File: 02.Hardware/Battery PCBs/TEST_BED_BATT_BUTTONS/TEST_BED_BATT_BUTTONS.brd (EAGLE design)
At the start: 25.2 x 30.9 mm, 9 parts

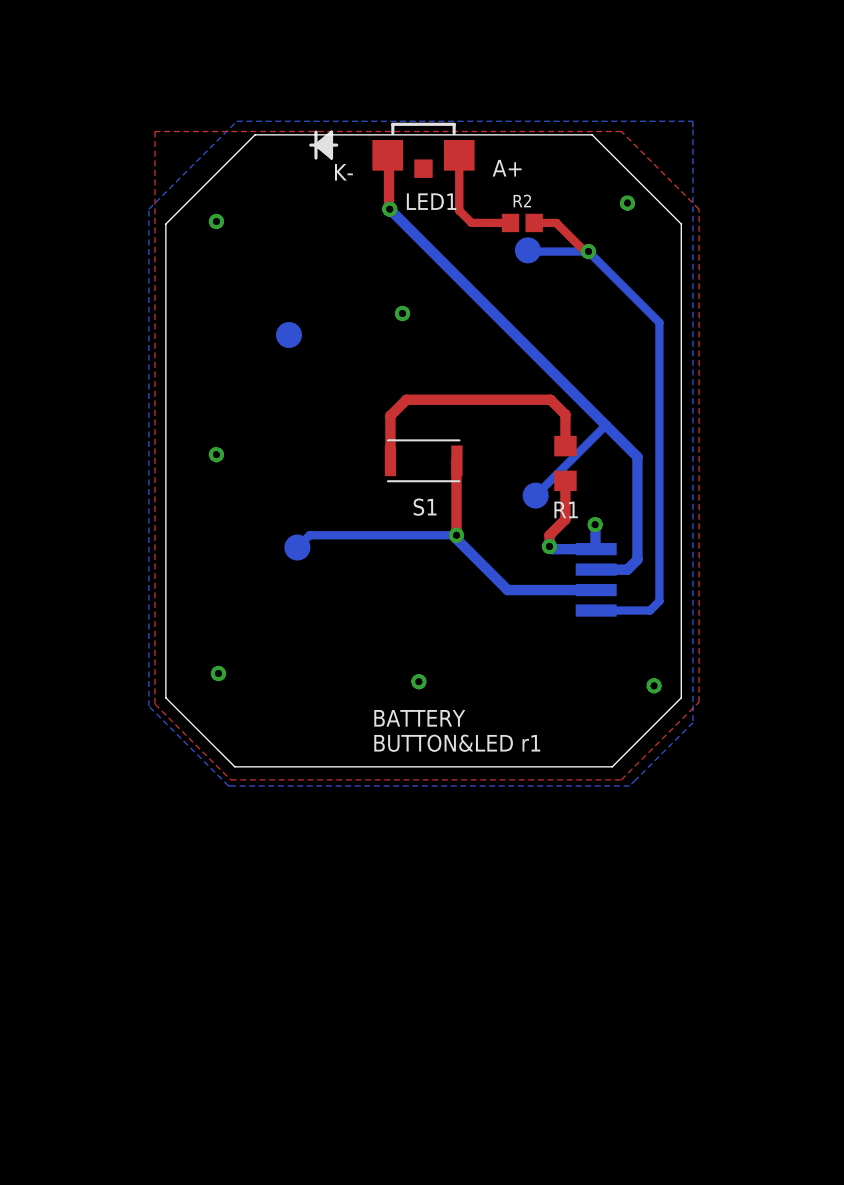
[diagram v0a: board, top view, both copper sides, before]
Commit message: Cambios revisados con David
Revision de los pcbs de la bateria.

En el DCDC se añade un diode Clamp (bat54s) en la medicion de la tension de salida.
Actualizacion de la BOM a v8.
Documentos de Cambios de versiones
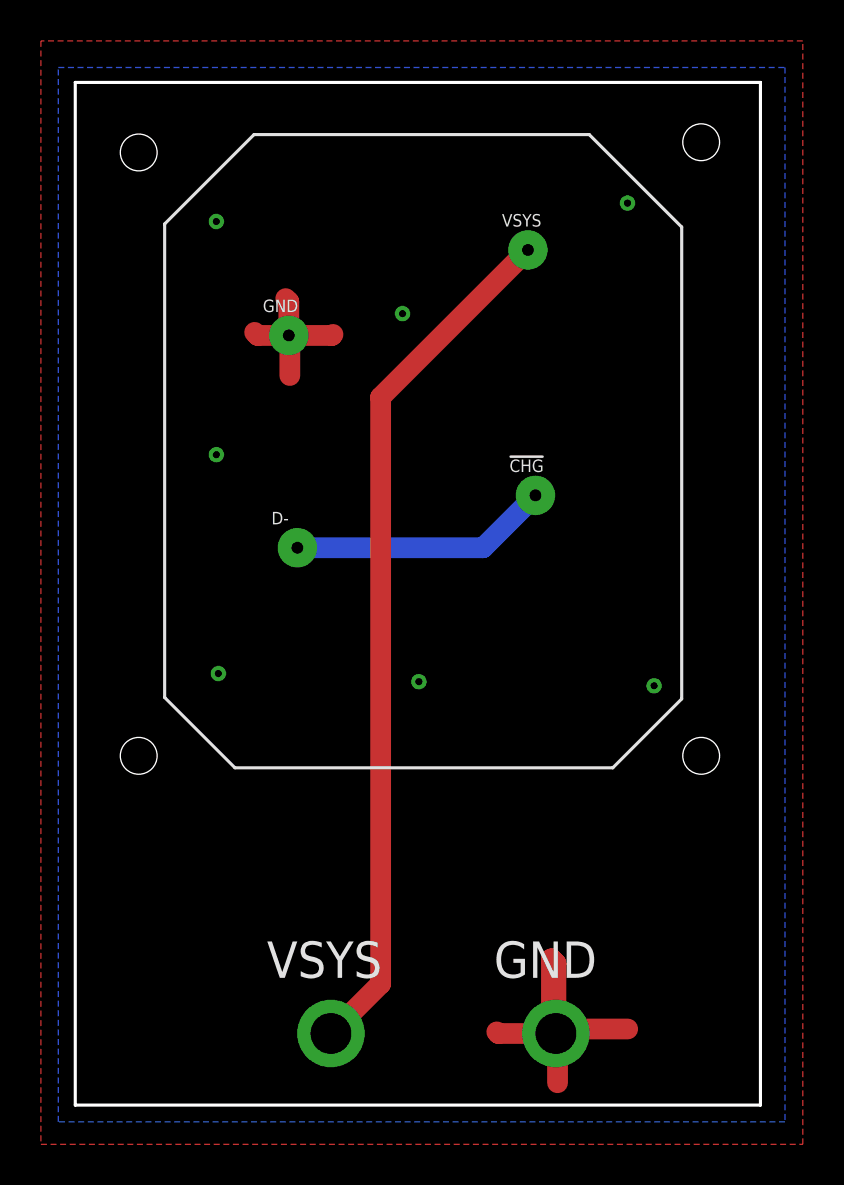
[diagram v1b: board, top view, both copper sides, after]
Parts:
- removed FLX1: FLEX4, Flex4:FLEX4
- removed LED1: APA3010SRCPRV-GX, APA3010 Led:LED_APA3010SRCPRV-GX_KNB
- removed R1: 1k, rcl:R0603
- removed R2: 2k2, SparkFun-Resistors:0402
- removed S1: KXT311LHS, switch momentary CK KXT311LHS:KXT311LHS
- added J1, J2: (no value), SparkFun-Connectors:1X01_2MM
- !CHG, D-, GND, VSYS: value TESTPAD_TPSQB1,27 -> (none); device BeagleBone_Blue_R3:TESTPAD_B1,27 -> SparkFun-Connectors:1X01_POGOPIN_HOLE_0.061_DIA
- flipped GND to the top
- flipped VSYS to the top
- flipped !CHG to the top
- flipped D- to the top
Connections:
- removed net !CHG!: !CHG.TP, FLX1.3, LED1.1
- removed net N$1: R1.2, S1.1
- removed net N$2: LED1.2, R2.1
- net D-: now also !CHG.2, D-.2; no longer D-.TP, FLX1.2, S1.2
- net GND: now also GND.2, J2.1; no longer FLX1.4, GND.TP, R1.1
- net VSYS: now also J1.1, VSYS.2; no longer FLX1.1, R2.2, VSYS.TP
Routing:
- net !CHG!: track 31.9 -> 0.00 mm, vias 1 -> 0
- net GND: track 7.09 -> 24.2 mm, vias 9 -> 7
- net VSYS: track 28.0 -> 42.3 mm, vias 1 -> 0
- net N$1: track 12.9 -> 0.00 mm
- net D-: track 19.7 -> 12.7 mm, vias 1 -> 0
- net N$2: track 5.46 -> 0.00 mm
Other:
- board size 25.2 x 30.9 mm -> 33.5 x 50 mm
- board text added: "GND"
- board text added: "TEST BED BUTTONS v1-May22"
- board text added: "VSYS"
- board text removed: "A+"
- board text removed: "BATTERY BUTTON&LED r1"
- board text removed: "K-"
